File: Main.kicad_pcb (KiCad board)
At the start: 2 copper layers, 59 parts, among them J1 Conn_02x06_Top_Bottom, J6 Conn_01x03, J7 Conn_01x03, J8 Conn_01x06, Q1 CSD17307Q5A, Q2 CSD17307Q5A, U1 LM4120-CustomSymbols, U2 LTC2942, U3 LM393, U4 TPS2557, U5 LM393, U6 TPS2557, U7 SN74LVC2G08

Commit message: started layout
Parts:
- moved R16 208.5 mm to (-37.4, 166.8)
- moved R22 208.5 mm to (-31.4, 168.9)
- moved C1 208.5 mm to (-49.3, 163.5)
- moved R17 208.5 mm to (-49.3, 170.1)
- moved R19 208.5 mm to (-43.3, 170.1)
- moved R3 208.5 mm to (-37.4, 163.5)
- moved BAT-1 204.9 mm to (-53.6, 131.0)
- moved C2 204.9 mm to (-13.3, 117.6)
- moved C3 204.9 mm to (-19.3, 117.6)
- moved GND1 204.9 mm to (-61.7, 131.0)
- moved J8 204.9 mm to (-82.8, 114.7)
- moved OUT1 204.9 mm to (-79.6, 129.6)
- moved R7 204.9 mm to (-37.1, 122.9)
- moved BAT+1 204.9 mm to (-57.6, 131.0)
- moved CDR1 204.9 mm to (-49.5, 135.0)
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
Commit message: worked on pcb
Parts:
- added C9: 1u, Capacitor_SMD:C_1206_3216Metric_Pad1.42x1.75mm_HandSolder, F.Cu at (171.9, 114.6)
- R17: value 56.2k -> 284k
- R19, R22: value 66.5k -> 332k
- R6: value 6k -> 4.87k
- moved C1 233.9 mm to (181.0, 122.3), turned to 90 degrees
- moved BT1 202.8 mm to (161.9, 89.7)
- moved U1 199.7 mm to (176.6, 122.4), turned to 270 degrees
- moved J6 191.3 mm to (119.2, 121.4)
- moved C4 135.3 mm to (208.6, 141.0), turned to 0 degrees
- moved R18 132.2 mm to (208.6, 138.2), turned to 0 degrees
- moved U4 126.6 mm to (204.2, 136.7), turned to 90 degrees
- moved R20 125.5 mm to (208.8, 131.7), turned to 0 degrees
- moved C5 121.9 mm to (208.8, 128.2), turned to 0 degrees
- moved D1 120.3 mm to (198.2, 135.7), turned to 90 degrees
- moved J7 119.7 mm to (124.9, 121.5)
- moved R21 118.3 mm to (208.8, 124.5), turned to 0 degrees
- moved R23 111.7 mm to (201.6, 125.0), turned to 270 degrees
- moved D2 111.3 mm to (198.2, 127.6), turned to 270 degrees
- moved U6 110.6 mm to (204.8, 120.8), turned to 0 degrees
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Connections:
- R17 pad 1: PACK+ -> 5Vref
- R19 pad 1: PACK+ -> 5Vref
- R22 pad 1: PACK+ -> 5Vref
- U3 pad 8: 5Vin -> PACK+
- U5 pad 8: 5Vin -> PACK+
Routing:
- net GNDD: track 0.00 -> 72.3 mm, vias 0 -> 4
- net TempOK: track 0.00 -> 66.1 mm
- net PACK+: track 0.00 -> 57.9 mm
- net GNDA: track 0.00 -> 44.1 mm, vias 0 -> 3
- net Net-(C5-Pad1): track 0.00 -> 39.6 mm
- net Net-(C7-Pad1): track 0.00 -> 38.8 mm
- net BatTemp: track 0.00 -> 35.7 mm
- net Net-(C6-Pad1): track 0.00 -> 23.0 mm
- net 5Vref: track 0.00 -> 17.3 mm
- net MPB: track 0.00 -> 14.0 mm
- net LowTemp: track 0.00 -> 13.7 mm
- net 1.4Vref: track 0.00 -> 10.2 mm
- net HighTemp: track 0.00 -> 6.93 mm
- net Net-(R21-Pad1): track 0.00 -> 1.82 mm
- added copper zone on F.Cu, net 5Vref
- added copper zone on B.Cu, net GNDA
- added copper zone on B.Cu, net GNDD
- added copper zone on F.Cu, net PACK+
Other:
- board outline added: 111.8 x 71.1 mm
- net class Small added: clearance 0.2, trace_width 0.2, via_dia 0.8, via_drill 0.4

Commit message: restarted
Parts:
- removed AL/CC1, BAT+1, BAT-1, PACK+1, SCL1, SDA1: TestPoint, Connector_PinHeader_2.00mm:PinHeader_1x01_P2.00mm_Vertical
- added J2: Conn_01x06_Male, Connector_PinSocket_2.00mm:PinSocket_1x06_P2.00mm_Vertical, F.Cu at (130.6, 154.4)
- moved C8 313.9 mm to (-103.4, 178.6), turned to 0 degrees
- moved R14 291.3 mm to (-86.4, 179.2), turned to 0 degrees
- moved R21 289.2 mm to (-74.5, 182.5)
- moved R15 286.7 mm to (-80.5, 179.2), turned to 0 degrees
- moved R13 285.4 mm to (-92.4, 182.7), turned to 0 degrees
- moved U5 284.2 mm to (-89.1, 171.1), turned to 0 degrees
- moved R20 280.6 mm to (-68.6, 174.8)
- moved R1 275.5 mm to (-92.4, 176.1), turned to 0 degrees
- moved R18 273.7 mm to (-62.6, 174.8)
- moved D1 272.8 mm to (-72.3, 170.5), turned to 0 degrees
- moved C1 272.7 mm to (-86.4, 175.9), turned to 0 degrees
- moved R23 270.2 mm to (-62.6, 181.4), turned to 0 degrees
- moved U4 268.0 mm to (-59.0, 187.3), turned to 0 degrees
- moved D2 266.0 mm to (-64.3, 170.5), turned to 0 degrees
- moved U6 265.6 mm to (-53.7, 181.8)
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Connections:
- net /BQ29707_P4 renamed BAT-1
- net Net-(BAT+1-Pad1) renamed BAT+1
- net Net-(OUT1-Pad1) renamed PACK+1
- U2 pad 3: Net-(SCL1-Pad1) -> SCL1
- U2 pad 4: Net-(SDA1-Pad1) -> SDA1
- U2 pad 5: Net-(AL/CC1-Pad1) -> AL_CC1
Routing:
- net BAT+1: track 0.00 -> 89.2 mm
- net TempOK: track 66.1 -> 0.00 mm
- net PACK+: track 57.9 -> 0.00 mm
- net BAT-1: track 0.00 -> 57.1 mm
- net GNDD: track 72.3 -> 16.3 mm, vias 4 -> 2
- net GNDA: track 44.1 -> 0.00 mm, vias 3 -> 0
- net Net-(C5-Pad1): track 39.6 -> 0.00 mm
- net Net-(C7-Pad1): track 38.8 -> 0.00 mm
- net BatTemp: track 35.7 -> 0.00 mm
- net /BQ29707_P2: track 0.00 -> 34.4 mm
- net /BQ29707_P3: track 0.00 -> 31.5 mm
- net /BQ29707_P5: track 0.00 -> 24.8 mm
- net Net-(Q1-Pad5): track 0.00 -> 24.2 mm
- net Net-(C6-Pad1): track 23.0 -> 0.00 mm
- net 5Vref: track 17.3 -> 0.00 mm
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- removed copper zone on F.Cu, net 5Vref
- removed copper zone on B.Cu, net GNDA
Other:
- board outline removed

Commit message: progress
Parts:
- moved C8 271.2 mm to (163.6, 131.0), turned to 270 degrees
- moved MPB1 266.0 mm to (167.8, 129.1)
- moved R21 236.0 mm to (155.8, 131.0), turned to 270 degrees
- moved R23 229.1 mm to (160.9, 131.0), turned to 270 degrees
- moved D2 228.0 mm to (158.4, 121.5), turned to 180 degrees
- moved D1 226.4 mm to (148.7, 121.5)
- moved R20 223.8 mm to (150.9, 131.0), turned to 270 degrees
- moved U6 217.5 mm to (157.0, 127.9), turned to 180 degrees
- moved U4 214.1 mm to (146.2, 126.0)
- moved GND1 213.8 mm to (71.8, 43.3)
- moved R1 213.8 mm to (66.6, 33.2)
- moved R11 213.8 mm to (102.3, 36.5)
- moved R12 213.8 mm to (108.3, 36.5)
- moved R13 213.8 mm to (66.6, 39.8)
- moved R14 213.8 mm to (72.6, 36.4)
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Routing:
- net BAT-1: track 57.1 -> 133.1 mm
- net GNDD: track 16.3 -> 49.5 mm, vias 2 -> 8
- net Net-(C6-Pad1): track 0.00 -> 32.6 mm
- net MPB: track 0.00 -> 18.6 mm
- net Net-(C5-Pad1): track 0.00 -> 12.7 mm, vias 0 -> 2
- net PACK+1: track 3.58 -> 15.6 mm
- net Net-(C7-Pad1): track 0.00 -> 12.0 mm, vias 0 -> 3
- net Net-(R21-Pad1): track 0.00 -> 8.65 mm, vias 0 -> 2
- net BAT+1: track 89.2 -> 96.3 mm, vias 0 -> 1
- net AL_CC1: track 0.00 -> 4.71 mm
- net SCL1: track 0.00 -> 3.44 mm
- net PACK+: track 0.00 -> 3.35 mm
- net SDA1: track 0.00 -> 3.08 mm
- net Net-(R20-Pad1): track 0.00 -> 3.03 mm
- net 5Vref: track 0.00 -> 2.36 mm

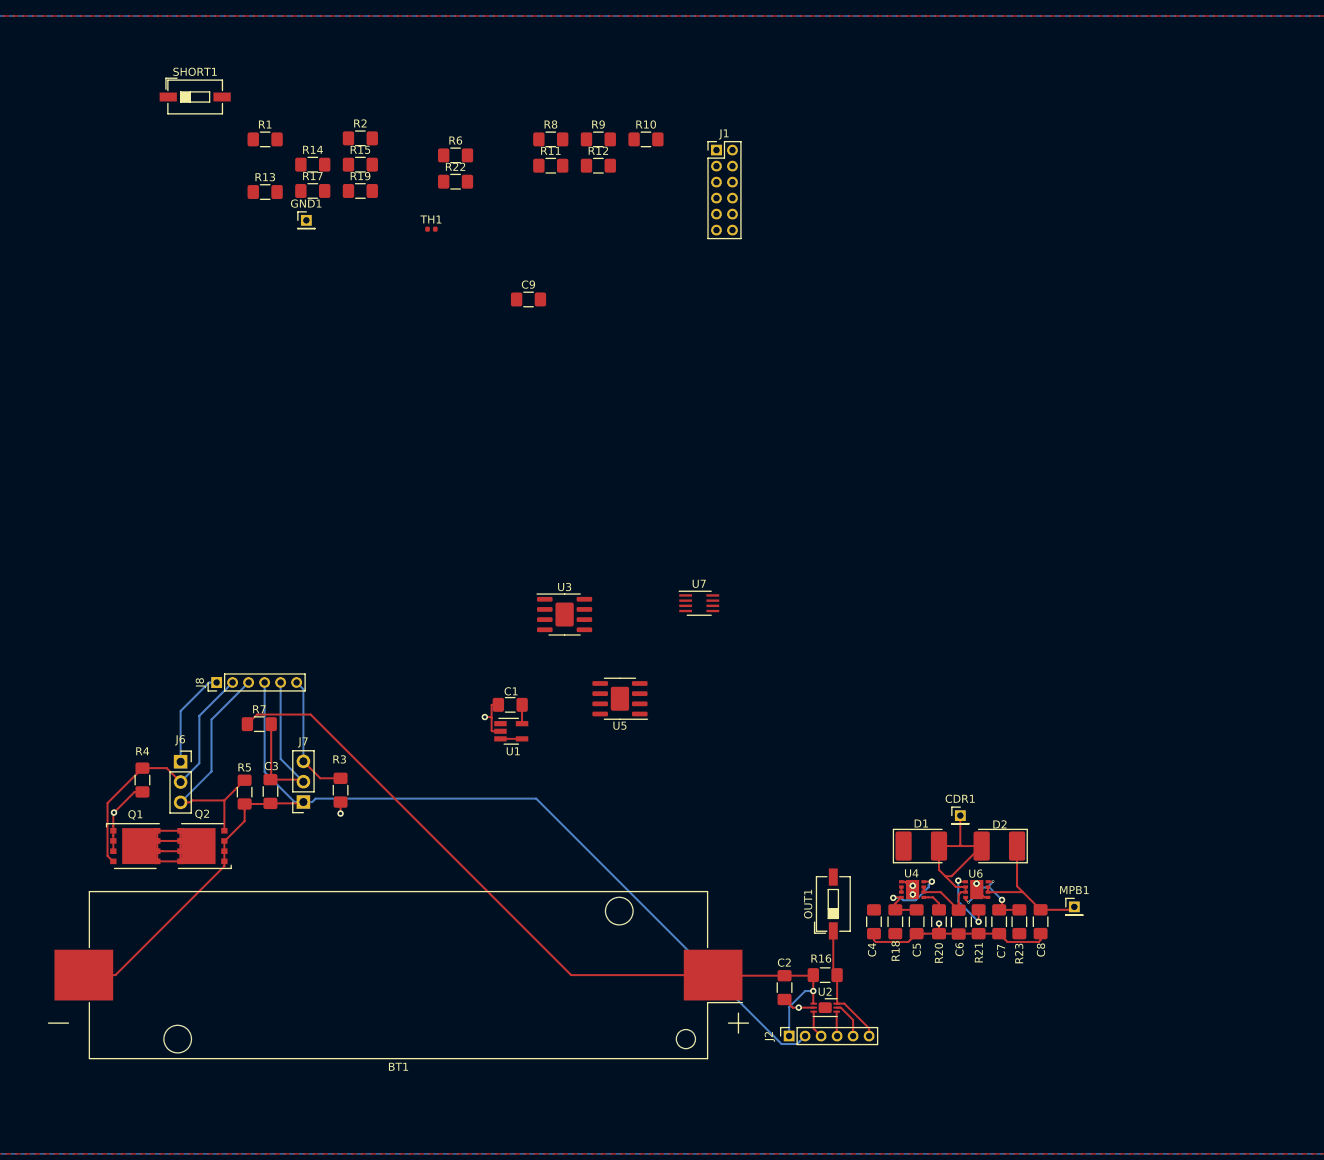
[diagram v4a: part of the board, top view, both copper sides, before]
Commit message: changed test points
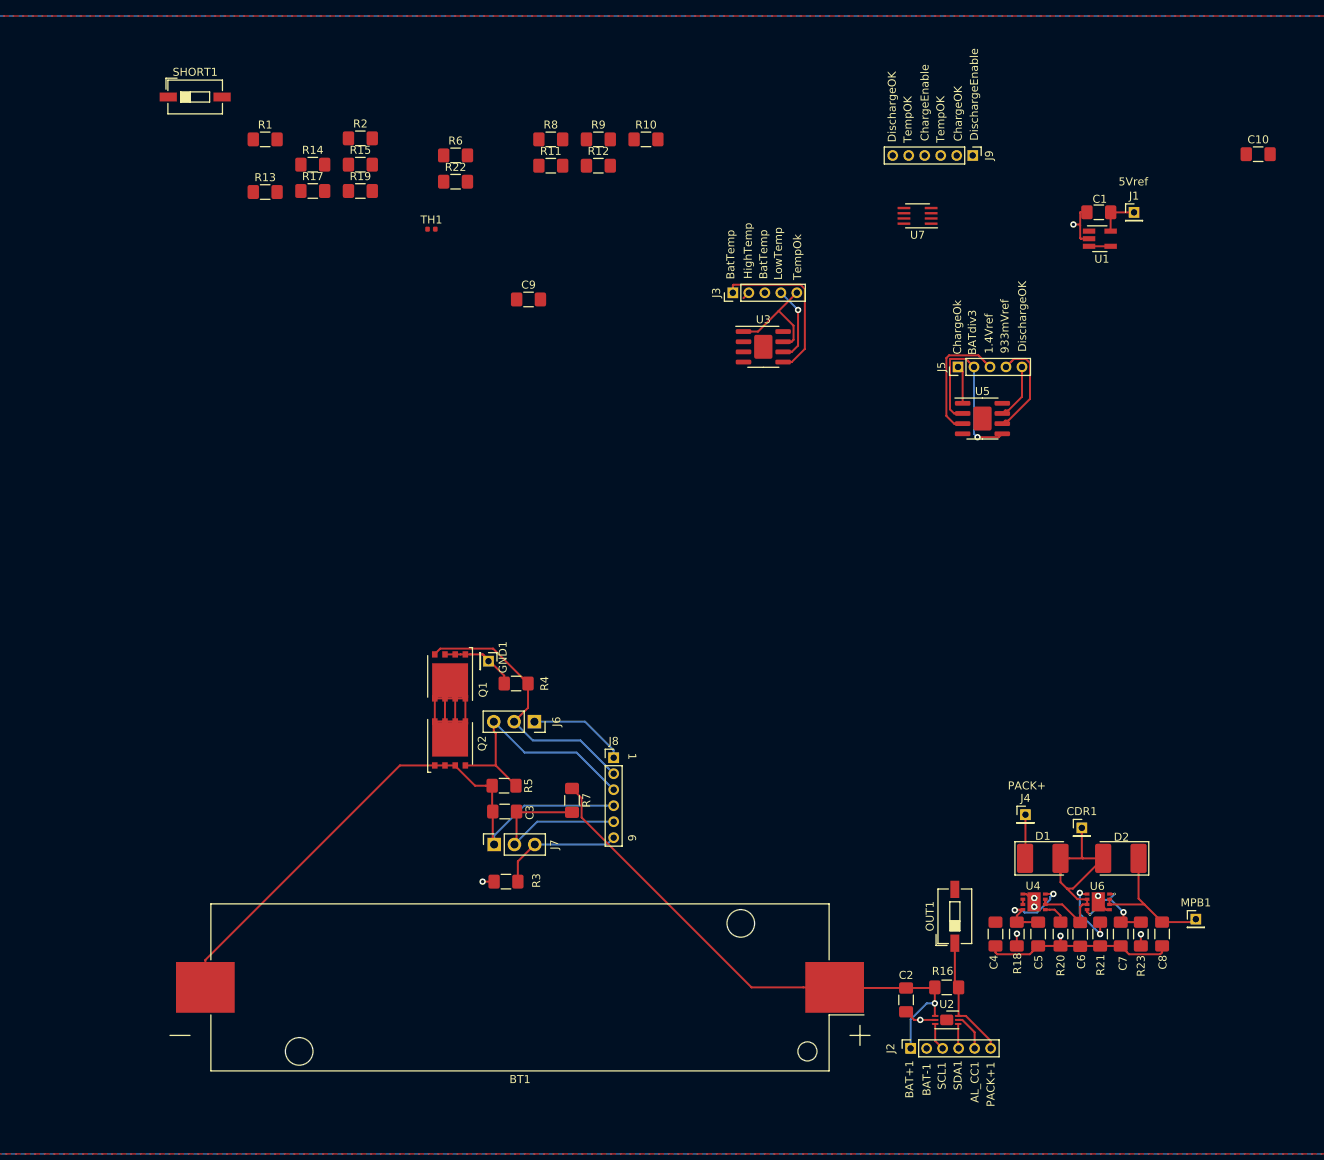
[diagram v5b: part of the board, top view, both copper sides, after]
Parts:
- added C10: 0.1u, Capacitor_SMD:C_1206_3216Metric_Pad1.42x1.75mm_HandSolder, F.Cu at (190.8, 35.1)
- added J3: Conn_01x05_Male, Connector_PinHeader_2.00mm:PinHeader_1x05_P2.00mm_Vertical, F.Cu at (125.1, 52.4)
- added J4: Conn_01x01_Male, Connector_PinHeader_2.00mm:PinHeader_1x01_P2.00mm_Vertical, F.Cu at (161.7, 117.6)
- added J5: Conn_01x05_Male, Connector_PinHeader_2.00mm:PinHeader_1x05_P2.00mm_Vertical, F.Cu at (153.3, 61.6)
- added J9: Conn_01x06_Male, Connector_PinHeader_2.00mm:PinHeader_1x06_P2.00mm_Vertical, F.Cu at (155.1, 35.2)
- J1: value Conn_02x06_Top_Bottom -> Conn_01x01_Male; footprint Connector_PinHeader_2.00mm:PinHeader_2x06_P2.00mm_Vertical -> Connector_PinHeader_2.00mm:PinHeader_1x01_P2.00mm_Vertical
- moved C1 95.9 mm to (170.9, 42.3)
- moved U1 95.9 mm to (171.0, 45.6)
- moved GND1 59.6 mm to (94.6, 98.4), turned to 270 degrees
- moved U5 57.3 mm to (156.3, 68.1), turned to 0 degrees
- moved U7 55.6 mm to (148.2, 42.8), turned to 180 degrees
- moved J1 52.8 mm to (175.3, 42.3)
- moved J8 50.5 mm to (110.2, 110.5), turned to 0 degrees
- moved R4 48.2 mm to (98.0, 101.2), turned to 0 degrees
- moved Q1 44.7 mm to (89.8, 100.3), turned to 270 degrees
- moved J6 44.5 mm to (100.3, 106.0), turned to 270 degrees
- moved U3 41.7 mm to (128.9, 59.1)
- moved R7 40.2 mm to (105.0, 115.8), turned to 270 degrees
- moved Q2 33.5 mm to (89.8, 108.7), turned to 90 degrees
- moved R5 32.4 mm to (96.5, 114.0), turned to 0 degrees
- moved C3 29.4 mm to (96.6, 117.2), turned to 180 degrees
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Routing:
- net BAT-1: track 133.1 -> 75.5 mm
- net BAT+1: track 96.3 -> 68.7 mm
- net BATdiv3: track 0.00 -> 23.7 mm, vias 0 -> 1
- net BatTemp: track 0.00 -> 21.1 mm
- net 1.4Vref: track 0.00 -> 15.9 mm
- net TempOK: track 0.00 -> 14.5 mm
- net 933mVref: track 0.00 -> 12.9 mm
- net LowTemp: track 0.00 -> 9.69 mm, vias 0 -> 1
- net DischargeOK: track 0.00 -> 7.06 mm
- net PACK+: track 3.35 -> 8.83 mm
- net ChargeOK: track 0.00 -> 4.79 mm
- net 5Vref: track 2.36 -> 5.28 mm
- net DischargeEnable: track 0.00 -> 1.54 mm, vias 0 -> 1
- net ChargeEnable: track 0.00 -> 1.46 mm, vias 0 -> 1
- net HighTemp: track 0.00 -> 0.95 mm
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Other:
- board text added: "1"
- board text added: "1.4Vref"
- board text added: "5Vref"
- board text added: "6"
- board text added: "933mVref"
- board text added: "AL_CC1"
- board text added: "BAT+1"
- board text added: "BAT-1"
- board text added: "BATdiv3"
- board text added: "BatTemp"
- board text added: "ChargeEnable"
- board text added: "ChargeOK"
- board text added: "ChargeOk"
- board text added: "DischargeEnable"
- board text added: "DischargeOK"
- board text added: "HighTemp"
- board text added: "LowTemp"
- board text added: "PACK+"
- board text added: "PACK+1"
- board text added: "SCL1"
- board text added: "SDA1"
- board text added: "TempOK"
- board text added: "TempOk"

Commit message: removed_switches
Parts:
- removed OUT1, SHORT1: SW_Push, Button_Switch_SMD:SW_DIP_SPSTx01_Slide_6.7x4.1mm_W6.73mm_P2.54mm_LowProfile_JPin
- added JP1: Jumper_2_Open, Connector_PinHeader_2.00mm:PinHeader_1x02_P2.00mm_Vertical, F.Cu at (141.3, 131.2)
- added JP2: Jumper_2_Open, Connector_PinHeader_2.00mm:PinHeader_1x02_P2.00mm_Vertical, F.Cu at (153.3, 133.7)
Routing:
- net BAT+1: track 68.7 -> 76.7 mm

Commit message: u-slot
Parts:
- JP1, JP2: footprint Connector_PinHeader_2.00mm:PinHeader_1x02_P2.00mm_Vertical -> Connector_PinSocket_2.54mm:PinSocket_1x02_P2.54mm_Vertical
- moved J1 62.4 mm to (183.7, 104.1), turned to 270 degrees
- moved C1 58.8 mm to (183.7, 99.7), turned to 90 degrees
- moved U1 55.1 mm to (180.4, 99.9), turned to 270 degrees
- moved JP1 1.89 mm to (142.3, 129.6)
- moved JP2 0.21 mm to (153.3, 133.5)
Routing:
- net BAT-1: track 75.5 -> 129.5 mm
- net BAT+1: track 76.7 -> 78.2 mm
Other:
- board outline added: 170.2 x 137.2 mm
- net class Battery Terminals added: clearance 0.2, trace_width 1, via_dia 0.8, via_drill 0.4

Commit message: progress
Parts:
- moved J1 7.70 mm to (183.1, 96.5)
- moved C1 5.96 mm to (180.1, 95.0)
- moved U1 0.83 mm to (180.8, 100.6), turned to 90 degrees
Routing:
- net GNDD: track 49.5 -> 46.6 mm, vias 7 -> 8
- net 5Vref: track 5.28 -> 7.60 mm
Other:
- outline, holes or cut-outs redrawn
- net class .75mm added: clearance 0.2, trace_width 0.75, via_dia 0.8, via_drill 0.4
